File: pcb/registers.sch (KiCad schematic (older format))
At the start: 5 parts

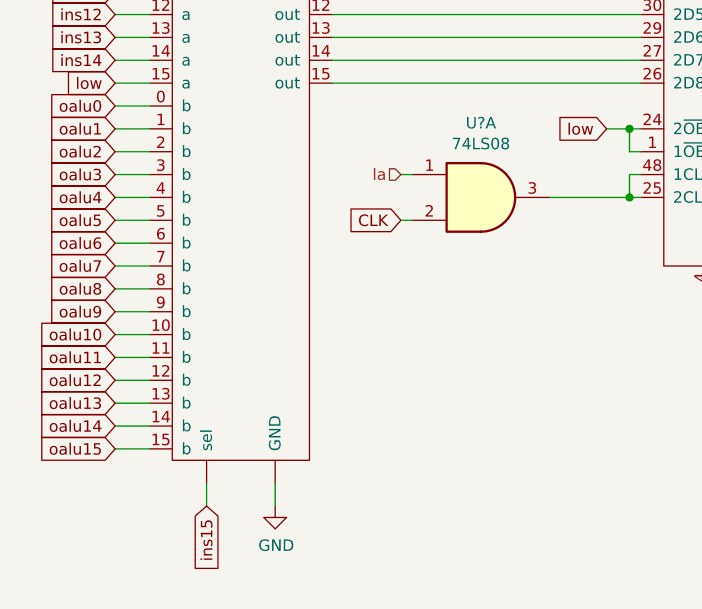
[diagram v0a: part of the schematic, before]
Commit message: instruction decoder and program counter
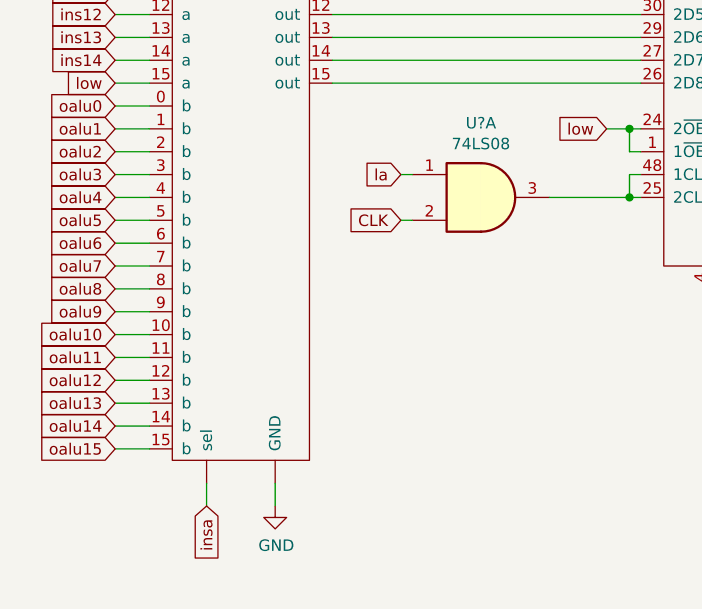
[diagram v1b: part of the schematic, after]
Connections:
- net ins15 renamed insa
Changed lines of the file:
@@
 EESchema Schematic File Version 4
 LIBS:cpu-cache
-EELAYER 26 0
+EELAYER 29 0
 EELAYER END
 $Descr A4 11693 8268
 encoding utf-8
-Sheet 2 2
+Sheet 2 5
 Title ""
 Date ""
@@
 Wire Wire Line
 	2300 3250 2350 3250
-Text HLabel 2300 3050 0    50   Input ~ 0
-la
 Wire Wire Line
 	2350 3050 2300 3050
@@
 Text GLabel 6200 2700 0    50   Input ~ 0
 oalu15
-Text GLabel 1450 4500 3    50   Input ~ 0
-ins15
 Text GLabel 7750 1200 2    50   Input ~ 0
 x0
@@
 	3950 950  4050 950
 Connection ~ 4050 950
+Text GLabel 2300 3050 0    50   Input ~ 0
+la
+Text GLabel 1450 4500 3    50   Input ~ 0
+insa
 $EndSCHEMATC

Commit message: flash mem
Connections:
- net CLK is gone; now on net clk: U?.2
- net ar0 renamed addr0
- net ar1 renamed addr1
- net ar10 renamed addr10
- net ar11 renamed addr11
- net ar12 renamed addr12
- net ar13 renamed addr13
- net ar14 renamed addr14
- net ar15 renamed addr15
- net ar2 renamed addr2
- net ar3 renamed addr3
- net ar4 renamed addr4
- net ar5 renamed addr5
- net ar6 renamed addr6
- net ar7 renamed addr7
- net ar8 renamed addr8
- net ar9 renamed addr9
- net x0 renamed dr0
- net x1 renamed dr1
- net x10 renamed dr10
- net x11 renamed dr11
- net x12 renamed dr12
- net x13 renamed dr13
- net x14 renamed dr14
- net x15 renamed dr15
- net x2 renamed dr2
- net x3 renamed dr3
- net x4 renamed dr4
- net x5 renamed dr5
- net x6 renamed dr6
- net x7 renamed dr7
- net x8 renamed dr8
- net x9 renamed dr9
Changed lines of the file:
@@
 	4600 2650 4700 2650
 Text GLabel 2300 3250 0    50   Input ~ 0
-CLK
+clk
 Wire Wire Line
 	2300 3250 2350 3250
@@
 Text GLabel 5350 3100 0    50   Input ~ 0
 ld
-Text GLabel 4700 1150 2    50   Input ~ 0
-ar0
-Text GLabel 4700 1250 2    50   Input ~ 0
-ar1
-Text GLabel 4700 1350 2    50   Input ~ 0
-ar2
-Text GLabel 4700 1450 2    50   Input ~ 0
-ar3
-Text GLabel 4700 1550 2    50   Input ~ 0
-ar4
-Text GLabel 4700 1650 2    50   Input ~ 0
-ar5
-Text GLabel 4700 1750 2    50   Input ~ 0
-ar6
-Text GLabel 4700 1850 2    50   Input ~ 0
-ar7
-Text GLabel 4700 1950 2    50   Input ~ 0
-ar8
-Text GLabel 4700 2050 2    50   Input ~ 0
-ar9
-Text GLabel 4700 2150 2    50   Input ~ 0
-ar10
-Text GLabel 4700 2250 2    50   Input ~ 0
-ar11
-Text GLabel 4700 2350 2    50   Input ~ 0
-ar12
-Text GLabel 4700 2450 2    50   Input ~ 0
-ar13
-Text GLabel 4700 2550 2    50   Input ~ 0
-ar14
-Text GLabel 4700 2650 2    50   Input ~ 0
-ar15
 Text GLabel 1050 1150 0    50   Input ~ 0
 ins0
@@
 Text GLabel 6200 2700 0    50   Input ~ 0
 oalu15
-Text GLabel 7750 1200 2    50   Input ~ 0
-x0
-Text GLabel 7750 1300 2    50   Input ~ 0
-x1
-Text GLabel 7750 1400 2    50   Input ~ 0
-x2
-Text GLabel 7750 1500 2    50   Input ~ 0
-x3
-Text GLabel 7750 1600 2    50   Input ~ 0
-x4
-Text GLabel 7750 1700 2    50   Input ~ 0
-x5
-Text GLabel 7750 1800 2    50   Input ~ 0
-x6
-Text GLabel 7750 1900 2    50   Input ~ 0
-x7
-Text GLabel 7750 2000 2    50   Input ~ 0
-x8
-Text GLabel 7750 2100 2    50   Input ~ 0
-x9
-Text GLabel 7750 2200 2    50   Input ~ 0
-x10
-Text GLabel 7750 2300 2    50   Input ~ 0
-x11
-Text GLabel 7750 2400 2    50   Input ~ 0
-x12
-Text GLabel 7750 2500 2    50   Input ~ 0
-x13
-Text GLabel 7750 2600 2    50   Input ~ 0
-x14
-Text GLabel 7750 2700 2    50   Input ~ 0
-x15
 Wire Wire Line
 	7600 1200 7750 1200
@@
 Text GLabel 1450 4500 3    50   Input ~ 0
 insa
+Text GLabel 7750 1200 2    50   Input ~ 0
+dr0
+Text GLabel 7750 1300 2    50   Input ~ 0
+dr1
+Text GLabel 7750 1400 2    50   Input ~ 0
+dr2
+Text GLabel 7750 1500 2    50   Input ~ 0
+dr3
+Text GLabel 7750 1600 2    50   Input ~ 0
+dr4
+Text GLabel 7750 1700 2    50   Input ~ 0
+dr5
+Text GLabel 7750 1800 2    50   Input ~ 0
+dr6
+Text GLabel 7750 1900 2    50   Input ~ 0
+dr7
+Text GLabel 7750 2000 2    50   Input ~ 0
+dr8
+Text GLabel 7750 2100 2    50   Input ~ 0
+dr9
+Text GLabel 7750 2200 2    50   Input ~ 0
+dr10
+Text GLabel 7750 2300 2    50   Input ~ 0
+dr11
+Text GLabel 7750 2400 2    50   Input ~ 0
+dr12
+Text GLabel 7750 2500 2    50   Input ~ 0
+dr13
+Text GLabel 7750 2600 2    50   Input ~ 0
+dr14
+Text GLabel 7750 2700 2    50   Input ~ 0
+dr15
+Text GLabel 4700 1150 2    50   Input ~ 0
+addr0
+Text GLabel 4700 1250 2    50   Input ~ 0
+addr1
+Text GLabel 4700 1350 2    50   Input ~ 0
+addr2
+Text GLabel 4700 1450 2    50   Input ~ 0
+addr3
+Text GLabel 4700 1550 2    50   Input ~ 0
+addr4
+Text GLabel 4700 1650 2    50   Input ~ 0
+addr5
+Text GLabel 4700 1750 2    50   Input ~ 0
+addr6
+Text GLabel 4700 1850 2    50   Input ~ 0
+addr7
+Text GLabel 4700 1950 2    50   Input ~ 0
+addr8
+Text GLabel 4700 2050 2    50   Input ~ 0
+addr9
+Text GLabel 4700 2150 2    50   Input ~ 0
+addr10
+Text GLabel 4700 2250 2    50   Input ~ 0
+addr11
+Text GLabel 4700 2350 2    50   Input ~ 0
+addr12
+Text GLabel 4700 2450 2    50   Input ~ 0
+addr13
+Text GLabel 4700 2550 2    50   Input ~ 0
+addr14
+Text GLabel 4700 2650 2    50   Input ~ 0
+addr15
 $EndSCHEMATC
